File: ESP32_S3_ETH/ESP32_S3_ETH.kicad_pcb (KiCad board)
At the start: 4 copper layers, 64.1 x 46 mm, 89 parts, among them IC1 TC1264-3.3VDB, J1 USB_C_Receptacle_USB2.0_16P, J2 USB_C_Receptacle_USB2.0_16P, J3 J1B1211CCD, Q1 L8050QLT1G, Q2 L8050QLT1G, SW1 RST, SW2 BOOT, U1 ESP32-S3-WROOM-1, U2 W5500, U3 CP2102N-A02-GQFN28, Y1 ECS-2033-250-BN-TR3

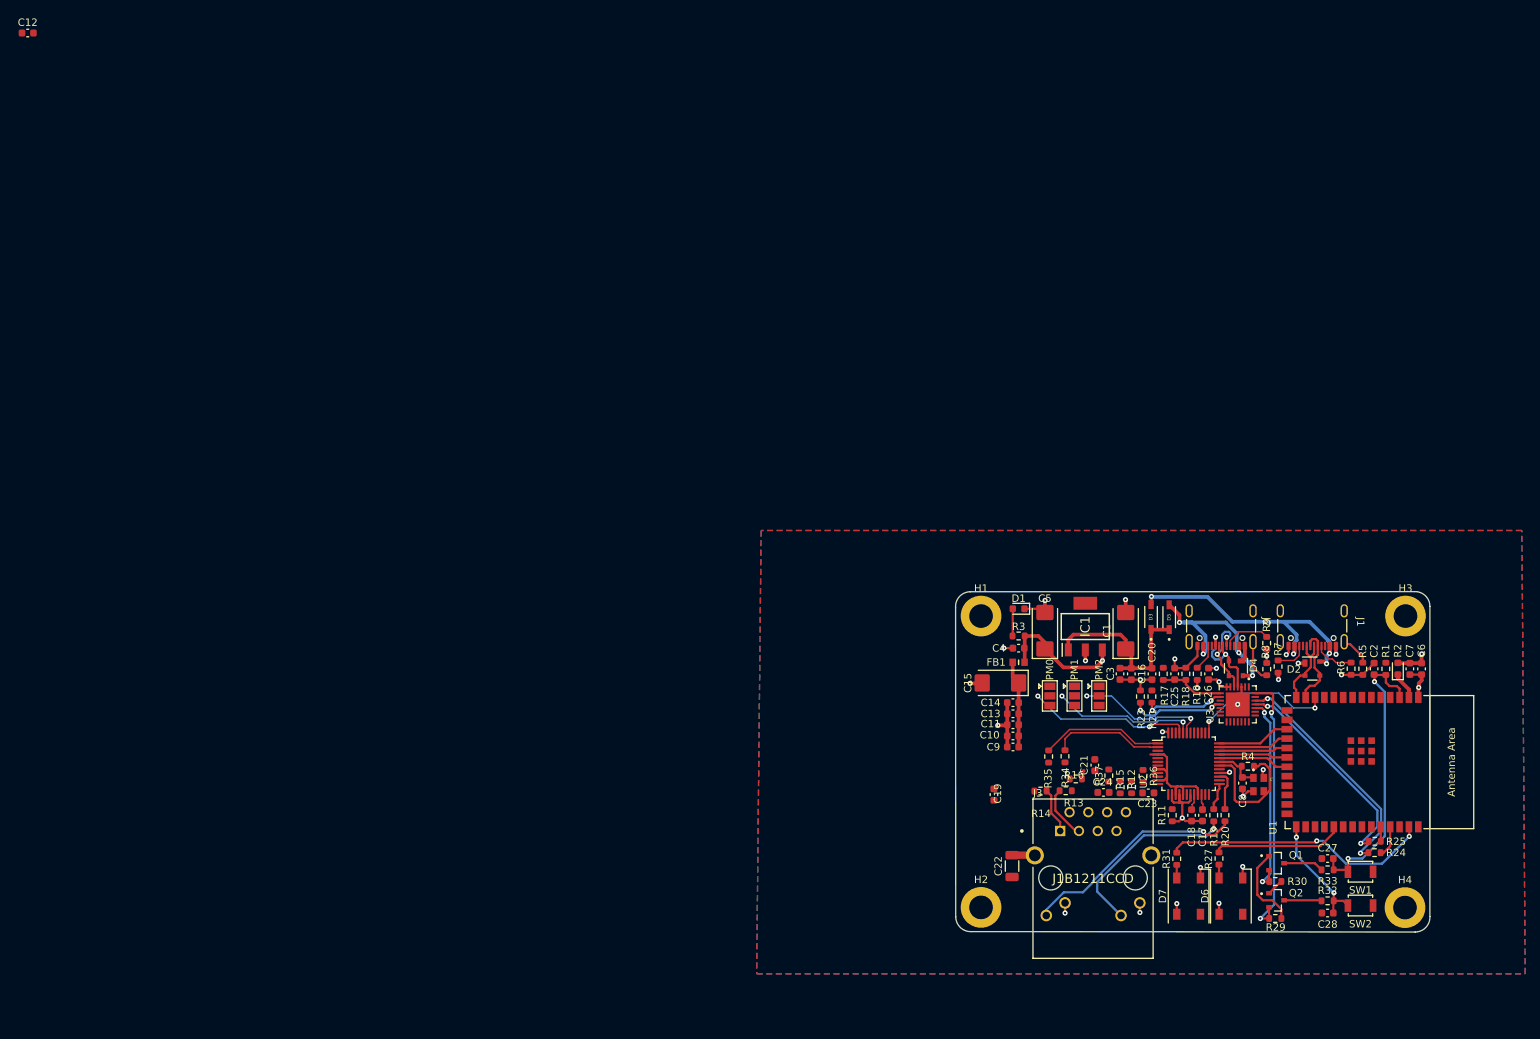
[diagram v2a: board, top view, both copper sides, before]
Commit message: Routing of Ethernet PCB completed, Pending further verification before finalized.
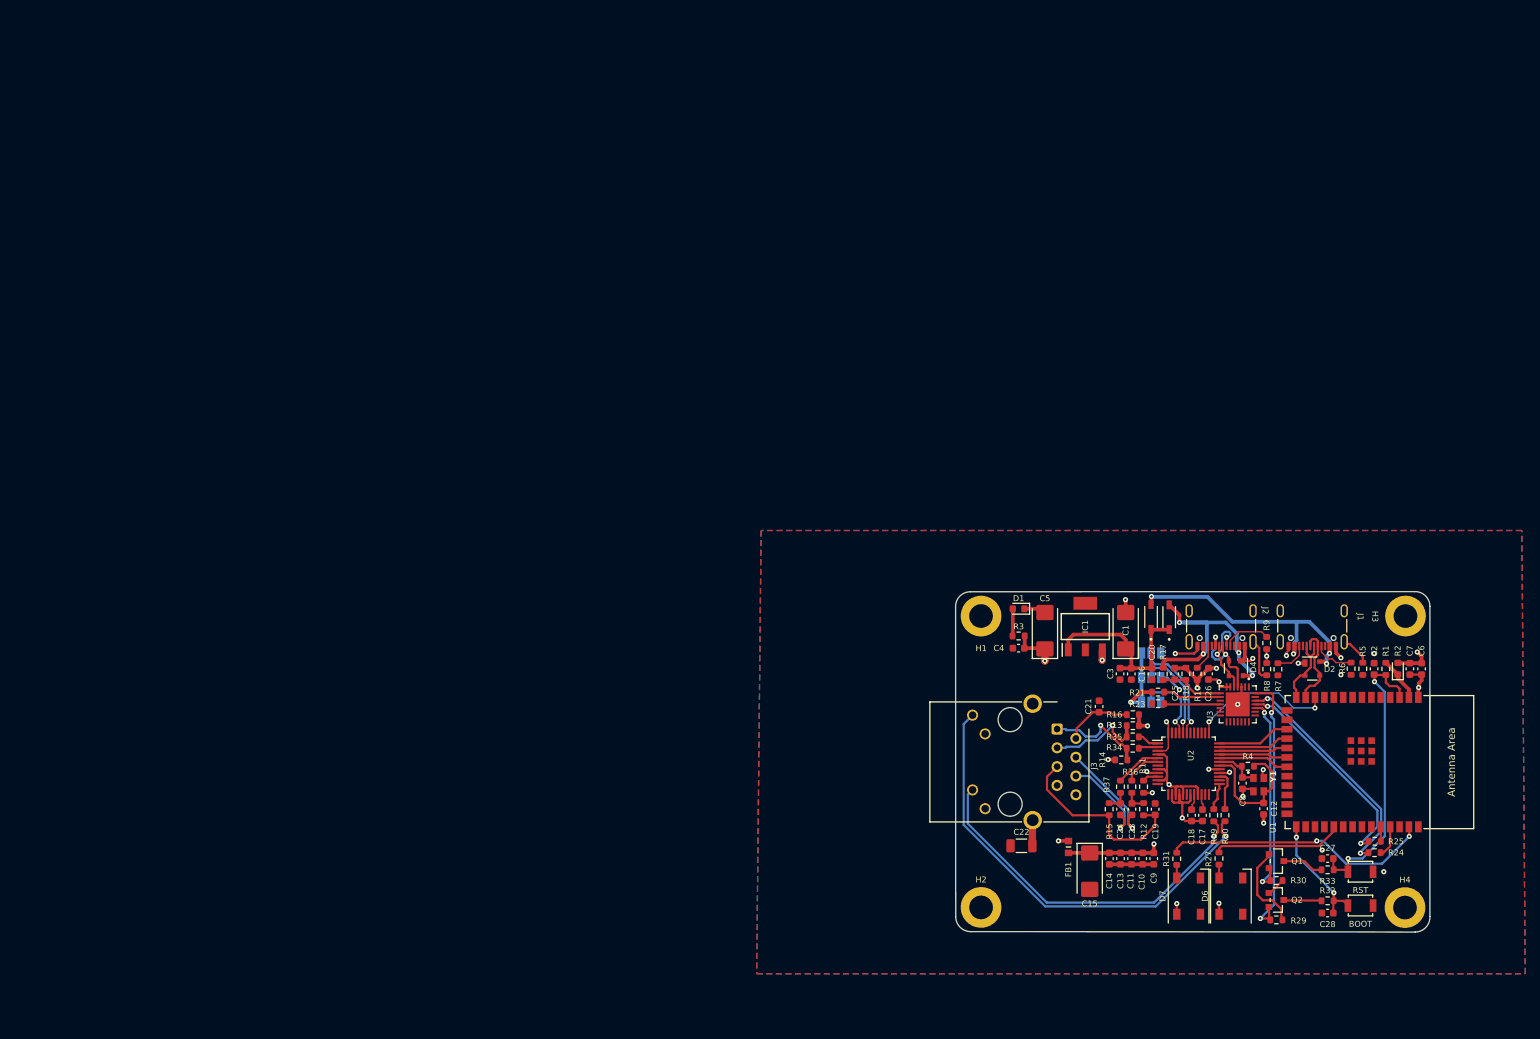
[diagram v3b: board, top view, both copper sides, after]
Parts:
- J3: footprint eec:WIZnet-J1B1211CCD-MFG -> Connector_RJ:RJ45_Cetus_J1B1211CCD_Horizontal
- PM0, PM1, PM2: moved to B.Cu
- Q1, Q2: footprint SS8050-G:TRANS_SS8050-G -> mmss8050:SOT-23_MCC
- moved C12 197.3 mm to (168.6, 105.7), turned to -90 degrees
- moved C15 28.2 mm to (145.1, 114.1), turned to -90 degrees
- moved FB1 25.9 mm to (142.2, 110.8), turned to -90 degrees
- moved C14 24.8 mm to (147.8, 112.4), turned to -90 degrees
- moved C13 24.4 mm to (149.3, 112.4), turned to -90 degrees
- moved C9 24.3 mm to (153.8, 112.4), turned to -90 degrees
- moved C11 24.2 mm to (150.8, 112.4), turned to -90 degrees
- moved C10 24.1 mm to (152.3, 112.4), turned to -90 degrees
- moved C19 21.9 mm to (154.0, 105.7), turned to 90 degrees
- moved J3 20.8 mm to (140.7, 94.9), turned to -90 degrees
- moved PM0 13.7 mm to (153.4, 91.2), turned to 0 degrees
- moved R13 12.6 mm to (150.9, 94.4)
- moved R14 11.7 mm to (149.4, 99.0)
- moved R35 11.7 mm to (150.9, 95.9), turned to 180 degrees
- moved R16 11.6 mm to (150.9, 92.9), turned to 180 degrees
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- renumbered SW2 to BOOT, SW1 to RST
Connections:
- C19 pad 1: /RJ_RX_N -> Net-(C19-Pad1)
- C24 pad 2: Net-(C24-Pad2) -> /RJ_RX_N
- J3 pad 5: /RJ_RX_N -> Net-(C19-Pad1)
- J3 pad 6: Net-(C24-Pad2) -> /RJ_RX_N
- R12 pad 2: /RJ_RX_N -> Net-(C19-Pad1)
- R15 pad 2: /RJ_RX_N -> Net-(C19-Pad1)
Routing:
- net /A3V3: track 28.7 -> 60.9 mm, vias 0 -> 4
- net Net-(J3-CATHODE_GREEN): track 30.7 -> 61.7 mm
- net Net-(C19-Pad1): track 0.00 -> 26.3 mm
- net /CH_GND: track 3.09 -> 27.8 mm
- net Net-(J3-CATHODE_YELLOW): track 25.8 -> 49.2 mm
- net Net-(J2-SHIELD): track 5.73 -> 22.7 mm
- net Net-(J1-SHIELD): track 4.34 -> 21.3 mm
- net /RJ_RX_P: track 0.51 -> 15.0 mm, vias 0 -> 1
- net /TX_N: track 16.7 -> 2.92 mm
- net /RJ_RX_N: track 0.00 -> 13.3 mm, vias 0 -> 1
- net /TX_P: track 15.2 -> 3.08 mm
- net /PMODE0: track 22.0 -> 10.7 mm, vias 2 -> 1
- net Net-(C21-Pad1): track 0.46 -> 9.13 mm
- net /V_BUS: track 27.4 -> 35.3 mm
- net /RJ_TX_P: track 6.16 -> 13.9 mm, vias 0 -> 1
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
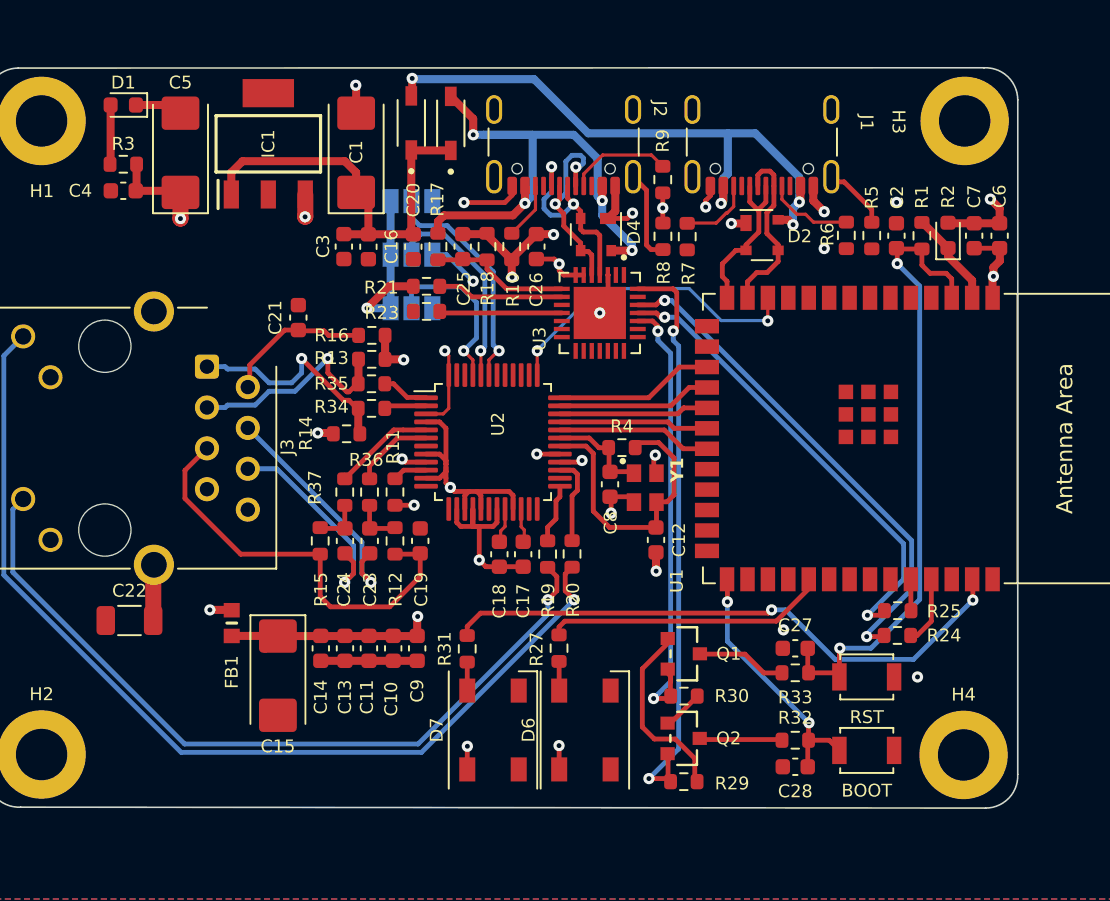
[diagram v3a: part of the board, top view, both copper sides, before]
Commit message: Ethernet PCB finalized and ordered, hardware construction pending arrival.
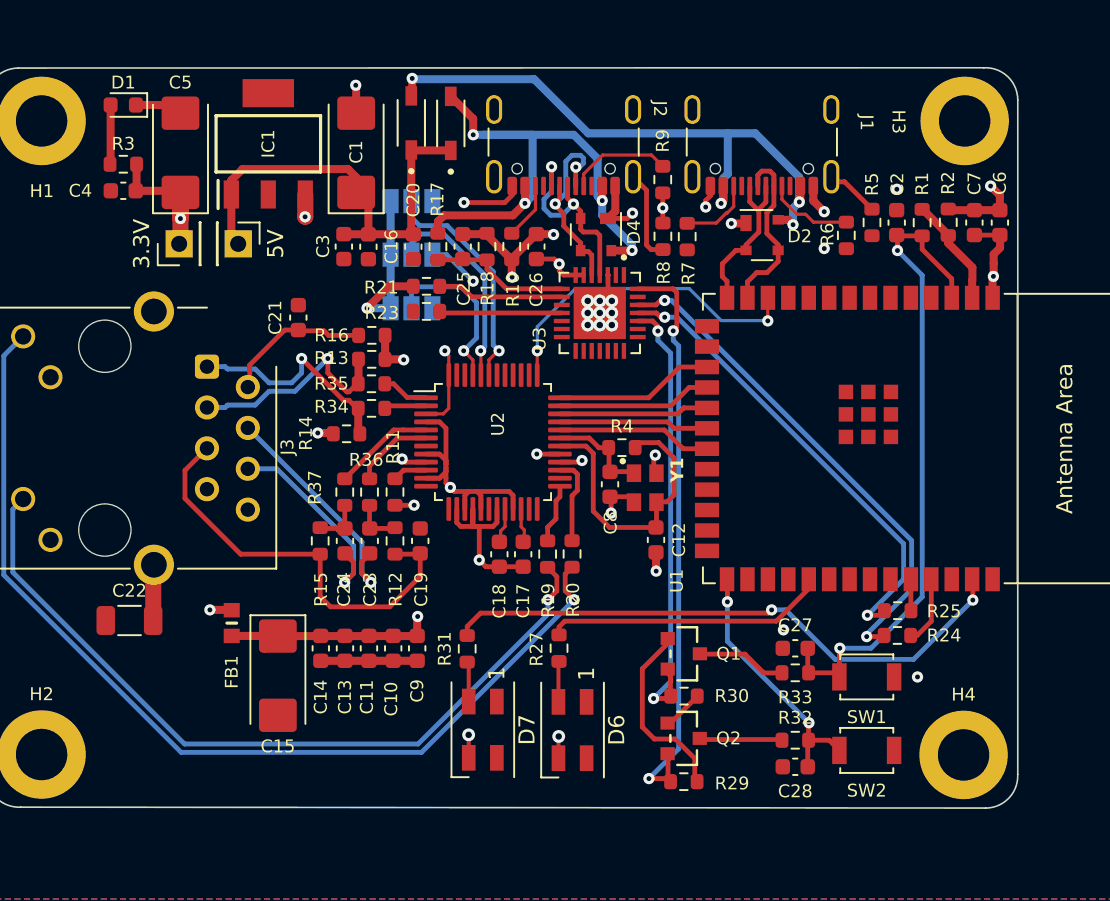
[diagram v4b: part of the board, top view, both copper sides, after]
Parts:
- added 3.3V: TestPoint, Connector_PinHeader_2.54mm:PinHeader_1x01_P2.54mm_Vertical, F.Cu at (139.0, 87.2)
- added 5V: TestPoint, Connector_PinHeader_2.54mm:PinHeader_1x01_P2.54mm_Vertical, F.Cu at (142.6, 87.2)
- added G***: LOGO, LOGO, B.Cu at (179.4, 99.2)
- added G***: LOGO, LOGO, B.Cu at (134.3, 99.3)
- added REF**: KiCad-Logo2_8mm_SilkScreen, Symbol:KiCad-Logo2_8mm_SilkScreen, B.Cu at (141.9, 112.6)
- D6, D7: footprint LED_SMD:LED_SK6812_PLCC4_5.0x5.0mm_P3.2mm -> LED_SMD:LED_SK6812MINI_PLCC4_3.5x3.5mm_P1.75mm
- R2: footprint Diode_SMD:D_0603_1608Metric -> Resistor_SMD:R_0603_1608Metric
- moved C2 0.81 mm to (183.6, 85.9)
- moved C6 0.81 mm to (190.0, 85.9)
- moved R1 0.81 mm to (185.2, 85.9)
- moved R2 0.81 mm to (186.8, 85.9)
- moved R5 0.81 mm to (182.1, 85.9)
- moved C7 0.81 mm to (188.4, 85.9)
- moved D6 0.77 mm to (163.4, 117.5), turned to -90 degrees
- moved D7 0.63 mm to (157.8, 117.5), turned to -90 degrees
- renumbered RST to SW1, BOOT to SW2
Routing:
- net /VCC_3V3: track 34.6 -> 37.7 mm
- net /VCC_5V: track 26.0 -> 28.4 mm
- net /CHIP_PU: track 40.0 -> 41.2 mm
- net /RSTn: track 19.7 -> 20.6 mm
- net GND: track 68.8 -> 69.6 mm, vias 23 -> 31
- net /ESP_3V3: track 6.00 -> 6.82 mm
- net Net-(J1-SHIELD): track 21.3 -> 20.6 mm
- net Net-(D7-DIN): track 1.78 -> 2.49 mm
- net Net-(D6-DIN): track 1.82 -> 2.53 mm
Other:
- board text added: "Designed by: Zachary Nicholson Theodore Tang V1.0"
- board text added: "https://github.com/znicholson17/P-Linked"
